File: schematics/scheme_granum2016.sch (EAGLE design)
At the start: 39 parts, among them U1 TSL2561T, U2 TSL2561T, U3 TSL2561T

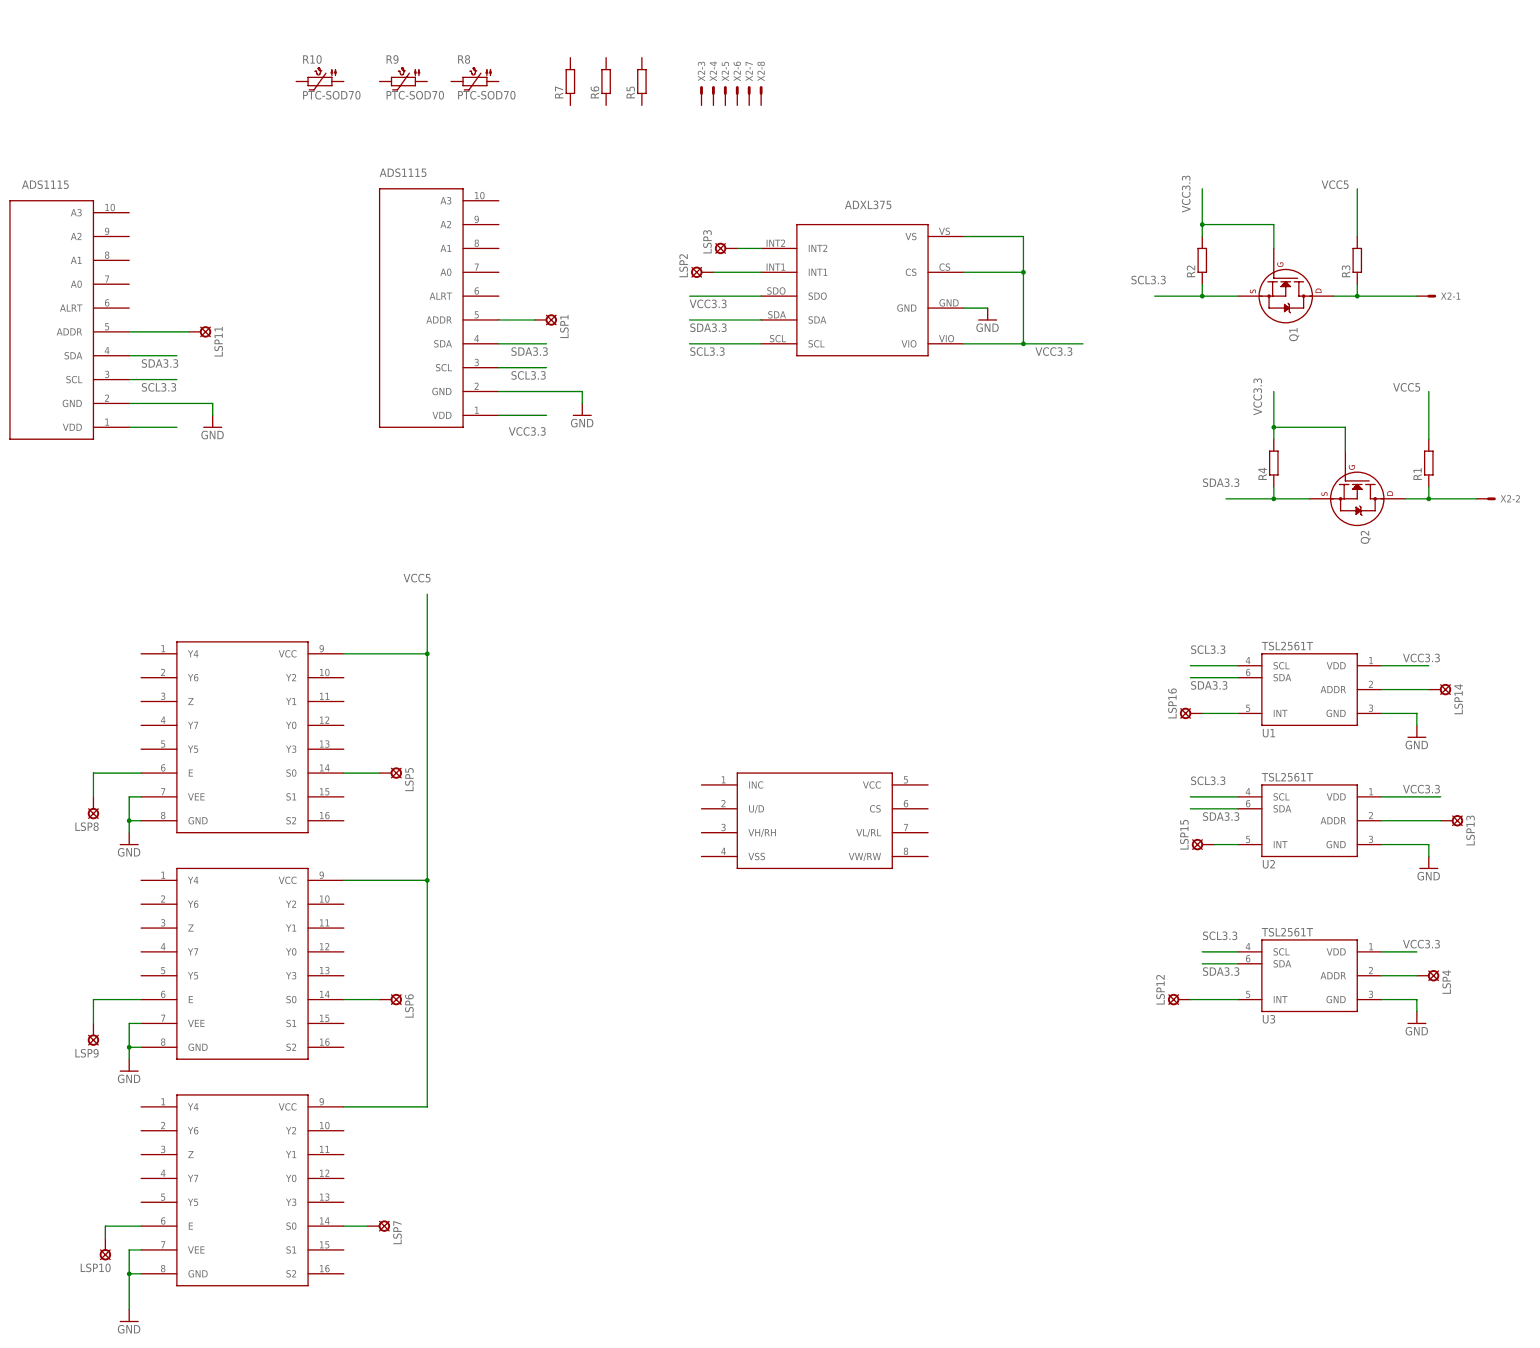
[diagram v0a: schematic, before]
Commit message: Немного подправила схему и добавила пьезо-пищалку с сервоприводом
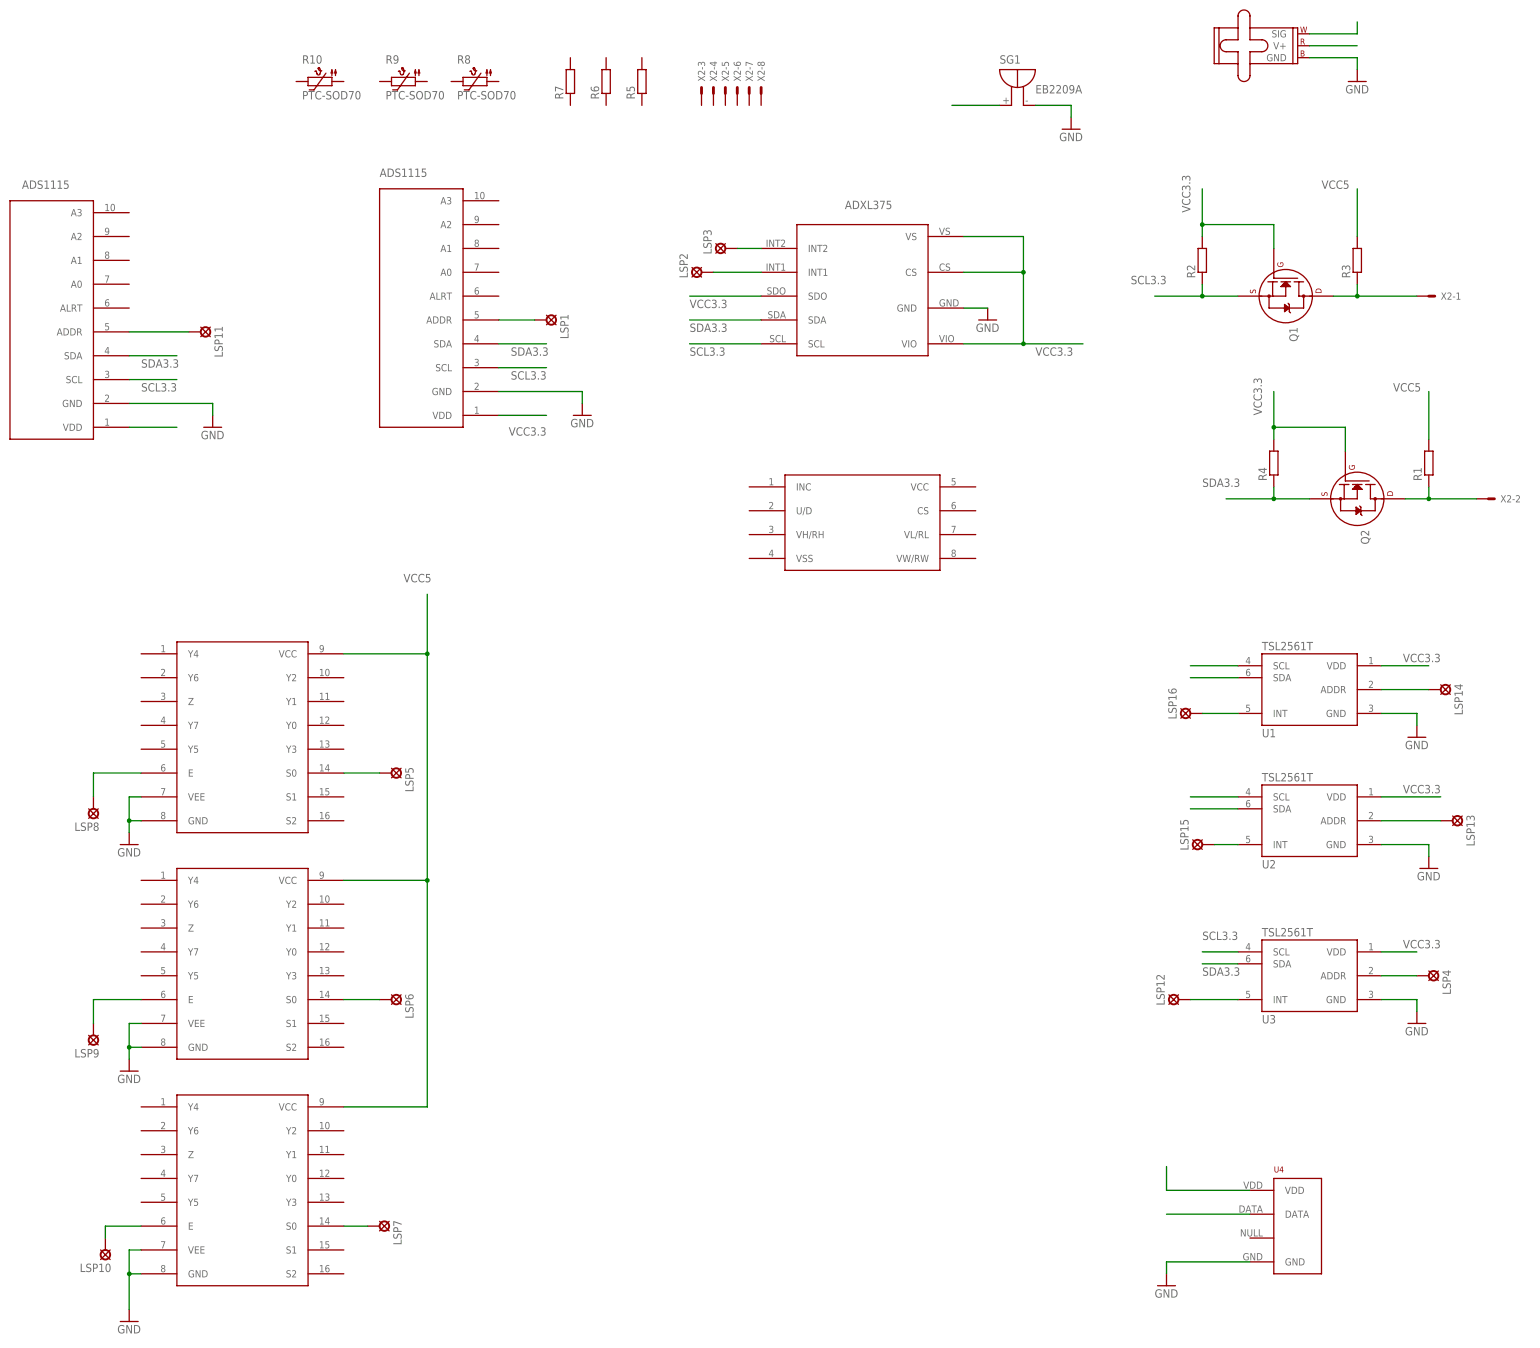
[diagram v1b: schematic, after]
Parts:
- added M1: SMALL_SERVO, SparkFun-Electromechanical:SMALL_SERVO
- added SG1: EB2209A, buzzer:EB2209A
- added U4: (no value), RHT03_DHT-22_AM2302:RHT03_DHT-22_AM2302RA
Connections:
- new net N$18: SG1.+
- new net N$19: U4.DATA
- new net N$25: M1.SIG
- new net SCL_5V: U1.SCL, U2.SCL
- net 5V: now also M1.V+, U4.VDD
- net GND: now also M1.GND, SG1.-, U4.GND
- net SCL_3.3V: no longer U1.SCL, U2.SCL
- net SDA_3.3V: no longer U1.SDA, U2.SDA
- net SDA_5V: now also U1.SDA, U2.SDA
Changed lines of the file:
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@@
 <part name="R9" library="ptc-ntc" deviceset="PTC-" device="SOD70"/>
 <part name="R10" library="ptc-ntc" deviceset="PTC-" device="SOD70"/>
+<part name="U4" library="RHT03_DHT-22_AM2302" deviceset="RHT03_DHT-22_AM2302" device="RA"/>
+<part name="GND10" library="supply1" deviceset="GND" device=""/>
+<part name="SG1" library="buzzer" deviceset="EB2209A" device=""/>
+<part name="GND11" library="supply1" deviceset="GND" device=""/>
+<part name="M1" library="SparkFun-Electromechanical" deviceset="SMALL_SERVO" device=""/>
+<part name="GND12" library="supply1" deviceset="GND" device=""/>
 </parts>
 <sheets>
@@
 <text x="116.84" y="-55.88" size="1.778" layer="95">SDA3.3</text>
 <text x="116.84" y="-48.26" size="1.778" layer="95">SCL3.3</text>
-<text x="114.3" y="-15.24" size="1.778" layer="95">SCL3.3</text>
-<text x="116.84" y="-22.86" size="1.778" layer="95">SDA3.3</text>
-<text x="114.3" y="12.7" size="1.778" layer="95">SCL3.3</text>
-<text x="114.3" y="5.08" size="1.778" layer="95">SDA3.3</text>
 <text x="167.64" y="-15.24" size="1.778" layer="95" rot="R180">VCC3.3</text>
 <text x="167.64" y="12.7" size="1.778" layer="95" rot="R180">VCC3.3</text>
@@
 <instance part="GND3" gate="1" x="162.56" y="-66.04"/>
 <instance part="LSP4" gate="1" x="165.1" y="-55.88" rot="R270"/>
-<instance part="U$3" gate="G$1" x="33.02" y="-22.86"/>
+<instance part="U$3" gate="G$1" x="43.18" y="40.64"/>
 <instance part="U$4" gate="G$1" x="-83.82" y="-101.6"/>
 <instance part="U$5" gate="G$1" x="-83.82" y="-5.08"/>
@@
 <instance part="R9" gate="G$1" x="-53.34" y="134.62"/>
 <instance part="R10" gate="G$1" x="-71.12" y="134.62"/>
+<instance part="U4" gate="G$1" x="137.16" y="-109.22"/>
+<instance part="GND10" gate="1" x="109.22" y="-121.92"/>
+<instance part="SG1" gate="G$1" x="76.2" y="132.08"/>
+<instance part="GND11" gate="1" x="88.9" y="124.46"/>
+<instance part="M1" gate="G$1" x="137.16" y="144.78"/>
+<instance part="GND12" gate="1" x="149.86" y="134.62"/>
 </instances>
 <busses>
@@
 <pinref part="U$7" gate="G$1" pin="SCL"/>
 <wire x1="-111.76" y1="71.12" x2="-101.6" y2="71.12" width="0.1524" layer="91"/>
-</segment>
-<segment>
-<pinref part="U2" gate="G$1" pin="SCL"/>
-<wire x1="124.46" y1="-17.78" x2="114.3" y2="-17.78" width="0.1524" layer="91"/>
-</segment>
-<segment>
-<pinref part="U1" gate="G$1" pin="SCL"/>
-<wire x1="124.46" y1="10.16" x2="114.3" y2="10.16" width="0.1524" layer="91"/>
 </segment>
 </net>
@@
 <pinref part="R1" gate="G$1" pin="2"/>
 </segment>
+<segment>
+<pinref part="U4" gate="G$1" pin="VDD"/>
+<wire x1="127" y1="-101.6" x2="109.22" y2="-101.6" width="0.1524" layer="91"/>
+<wire x1="109.22" y1="-101.6" x2="109.22" y2="-96.52" width="0.1524" layer="91"/>
+</segment>
+<segment>
+<pinref part="M1" gate="G$1" pin="V+"/>
+<wire x1="139.7" y1="142.24" x2="149.86" y2="142.24" width="0.1524" layer="91"/>
+</segment>
 </net>
 <net name="SDA_5V" class="0">
@@
 <wire x1="132.08" y1="48.26" x2="132.08" y2="45.72" width="0.1524" layer="91"/>
 <junction x="132.08" y="45.72"/>
+</segment>
+<segment>
+<pinref part="U1" gate="G$1" pin="SDA"/>
+<wire x1="124.46" y1="7.62" x2="114.3" y2="7.62" width="0.1524" layer="91"/>
+</segment>
+<segment>
+<pinref part="U2" gate="G$1" pin="SDA"/>
+<wire x1="124.46" y1="-20.32" x2="114.3" y2="-20.32" width="0.1524" layer="91"/>
 </segment>
 </net>
@@
 <pinref part="GND9" gate="1" pin="GND"/>
 </segment>
+<segment>
+<pinref part="U4" gate="G$1" pin="GND"/>
+<wire x1="127" y1="-116.84" x2="109.22" y2="-116.84" width="0.1524" layer="91"/>
+<wire x1="109.22" y1="-116.84" x2="109.22" y2="-119.38" width="0.1524" layer="91"/>
+<pinref part="GND10" gate="1" pin="GND"/>
+</segment>
+<segment>
+<pinref part="SG1" gate="G$1" pin="-"/>
+<wire x1="81.28" y1="129.54" x2="88.9" y2="129.54" width="0.1524" layer="91"/>
+<wire x1="88.9" y1="129.54" x2="88.9" y2="127" width="0.1524" layer="91"/>
+<pinref part="GND11" gate="1" pin="GND"/>
+</segment>
+<segment>
+<pinref part="M1" gate="G$1" pin="GND"/>
+<wire x1="139.7" y1="139.7" x2="149.86" y2="139.7" width="0.1524" layer="91"/>
+<wire x1="149.86" y1="139.7" x2="149.86" y2="137.16" width="0.1524" layer="91"/>
+<pinref part="GND12" gate="1" pin="GND"/>
+</segment>
 </net>
 <net name="SDA_3.3V" class="0">
@@
 <pinref part="U$7" gate="G$1" pin="SDA"/>
 <wire x1="-111.76" y1="76.2" x2="-101.6" y2="76.2" width="0.1524" layer="91"/>
-</segment>
-<segment>
-<pinref part="U2" gate="G$1" pin="SDA"/>
-<wire x1="124.46" y1="-20.32" x2="114.3" y2="-20.32" width="0.1524" layer="91"/>
-</segment>
-<segment>
-<pinref part="U1" gate="G$1" pin="SDA"/>
-<wire x1="124.46" y1="7.62" x2="114.3" y2="7.62" width="0.1524" layer="91"/>
 </segment>
 </net>
@@
 </segment>
 </net>
+<net name="SCL_5V" class="0">
+<segment>
+<pinref part="U1" gate="G$1" pin="SCL"/>
+<wire x1="124.46" y1="10.16" x2="114.3" y2="10.16" width="0.1524" layer="91"/>
+</segment>
+<segment>
+<pinref part="U2" gate="G$1" pin="SCL"/>
+<wire x1="124.46" y1="-17.78" x2="114.3" y2="-17.78" width="0.1524" layer="91"/>
+</segment>
+</net>
+<net name="N$19" class="0">
+<segment>
+<pinref part="U4" gate="G$1" pin="DATA"/>
+<wire x1="127" y1="-106.68" x2="109.22" y2="-106.68" width="0.1524" layer="91"/>
+</segment>
+</net>
+<net name="N$18" class="0">
+<segment>
+<pinref part="SG1" gate="G$1" pin="+"/>
+<wire x1="73.66" y1="129.54" x2="63.5" y2="129.54" width="0.1524" layer="91"/>
+</segment>
+</net>
+<net name="N$25" class="0">
+<segment>
+<pinref part="M1" gate="G$1" pin="SIG"/>
+<wire x1="139.7" y1="144.78" x2="149.86" y2="144.78" width="0.1524" layer="91"/>
+<wire x1="149.86" y1="144.78" x2="149.86" y2="147.32" width="0.1524" layer="91"/>
+</segment>
+</net>
